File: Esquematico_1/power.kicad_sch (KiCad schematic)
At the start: 22 parts, among them U6 TPS54302DDCR, U7 AP2112K-3.3TRG1

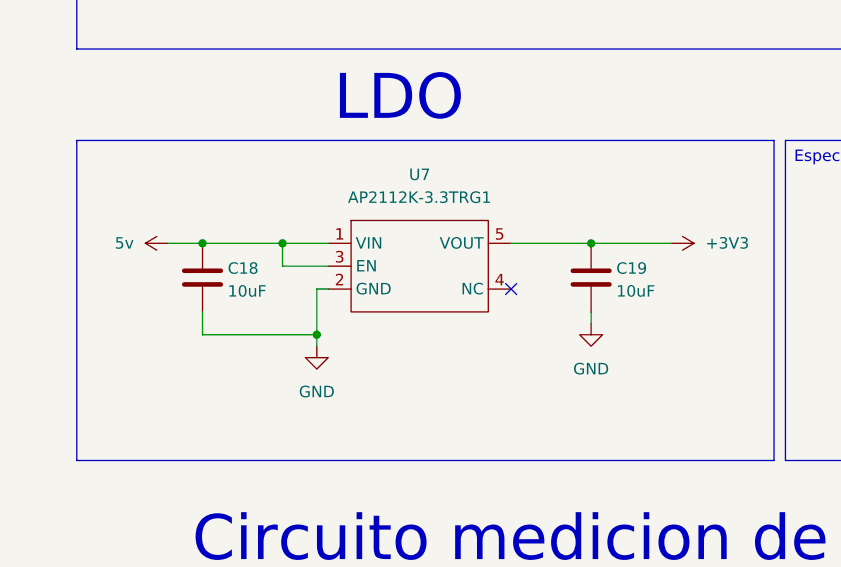
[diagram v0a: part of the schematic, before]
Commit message: Cambio del cristal por n-ésima vez
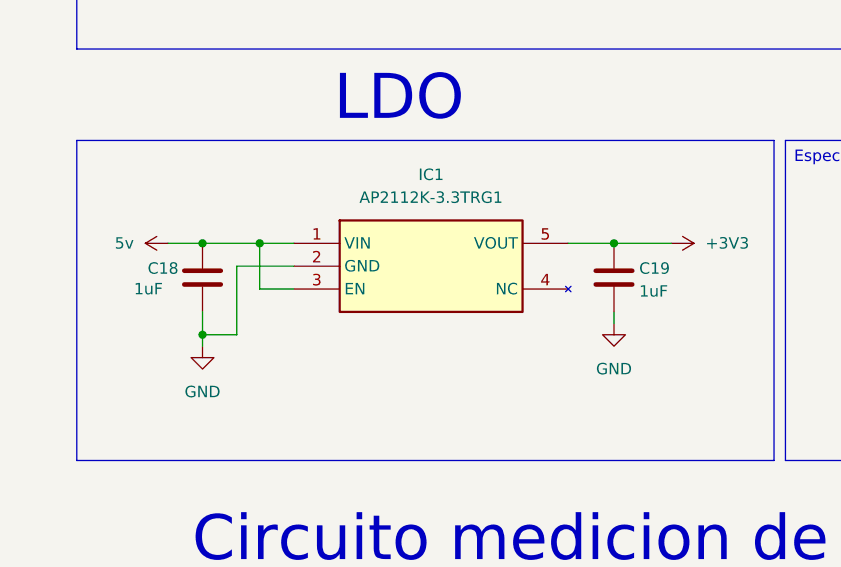
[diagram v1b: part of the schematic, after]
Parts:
- removed U7: AP2112K-3.3TRG1, AP2112K-3.3TRG1:SOT-23-6_L2.9-W1.6-P0.95-LS2.8-BL, symbol AP2112K-3.3TRG1:AP2112K-3.3TRG1_C23380830
- added IC1: AP2112K-3.3TRG1, AP2112K-3.3TRG1:SOT95P285X140-5N, symbol AP2112K-3_3TRG1:AP2112K-3.3TRG1
- C12, C13, C14, C15, C33: footprint (none) -> Capacitor_SMD:C_0805_2012Metric_Pad1.18x1.45mm_HandSolder
- C18, C19: value 10uF -> 1uF; footprint (none) -> Capacitor_SMD:C_0805_2012Metric_Pad1.18x1.45mm_HandSolder
- D1: footprint (none) -> Package_TO_SOT_SMD:SOT-23
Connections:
- net +3V3: now also IC1.5 (VOUT)
- net 5v: now also IC1.1 (VIN), IC1.3 (EN)
- net GND: now also IC1.2 (GND)
- no-connect marks 1 -> 0
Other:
- moved on the sheet: C19

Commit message: Footprints
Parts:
- C16, C17: footprint (none) -> Capacitor_SMD:C_0805_2012Metric_Pad1.18x1.45mm_HandSolder
- L1: footprint (none) -> Inductor_SMD:L_KOHERelec_MDA7030
- R10, R11, R12, R13, R17, R18, R9: footprint (none) -> Resistor_SMD:R_0805_2012Metric_Pad1.20x1.40mm_HandSolder
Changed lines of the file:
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@@
 			)
 		)
-		(property "Footprint" ""
+		(property "Footprint" "Inductor_SMD:L_KOHERelec_MDA7030"
 			(at 120.65 46.99 0)
 			(effects
@@
 			)
 		)
-		(property "Footprint" ""
+		(property "Footprint" "Resistor_SMD:R_0805_2012Metric_Pad1.20x1.40mm_HandSolder"
 			(at 156.972 59.69 90)
 			(effects
@@
 			)
 		)
-		(property "Footprint" ""
+		(property "Footprint" "Capacitor_SMD:C_0805_2012Metric_Pad1.18x1.45mm_HandSolder"
 			(at 133.6548 50.8 0)
 			(effects
@@
 			)
 		)
-		(property "Footprint" ""
+		(property "Footprint" "Resistor_SMD:R_0805_2012Metric_Pad1.20x1.40mm_HandSolder"
 			(at 156.972 68.58 90)
 			(effects
@@
 			)
 		)
-		(property "Footprint" ""
+		(property "Footprint" "Capacitor_SMD:C_0805_2012Metric_Pad1.18x1.45mm_HandSolder"
 			(at 127.3048 50.8 0)
 			(effects
@@
 			)
 		)
-		(property "Footprint" ""
+		(property "Footprint" "Resistor_SMD:R_0805_2012Metric_Pad1.20x1.40mm_HandSolder"
 			(at 68.072 162.56 90)
 			(effects
@@
 			)
 		)
-		(property "Footprint" ""
+		(property "Footprint" "Resistor_SMD:R_0805_2012Metric_Pad1.20x1.40mm_HandSolder"
 			(at 63.5 157.988 90)
 			(effects
@@
 			)
 		)
-		(property "Footprint" ""
+		(property "Footprint" "Resistor_SMD:R_0805_2012Metric_Pad1.20x1.40mm_HandSolder"
 			(at 50.292 46.99 90)
 			(effects
@@
 			)
 		)
-		(property "Footprint" ""
+		(property "Footprint" "Resistor_SMD:R_0805_2012Metric_Pad1.20x1.40mm_HandSolder"
 			(at 156.972 50.8 90)
 			(effects
@@
 			)
 		)
-		(property "Footprint" ""
+		(property "Footprint" "Resistor_SMD:R_0805_2012Metric_Pad1.20x1.40mm_HandSolder"
 			(at 50.292 36.83 90)
 			(effects

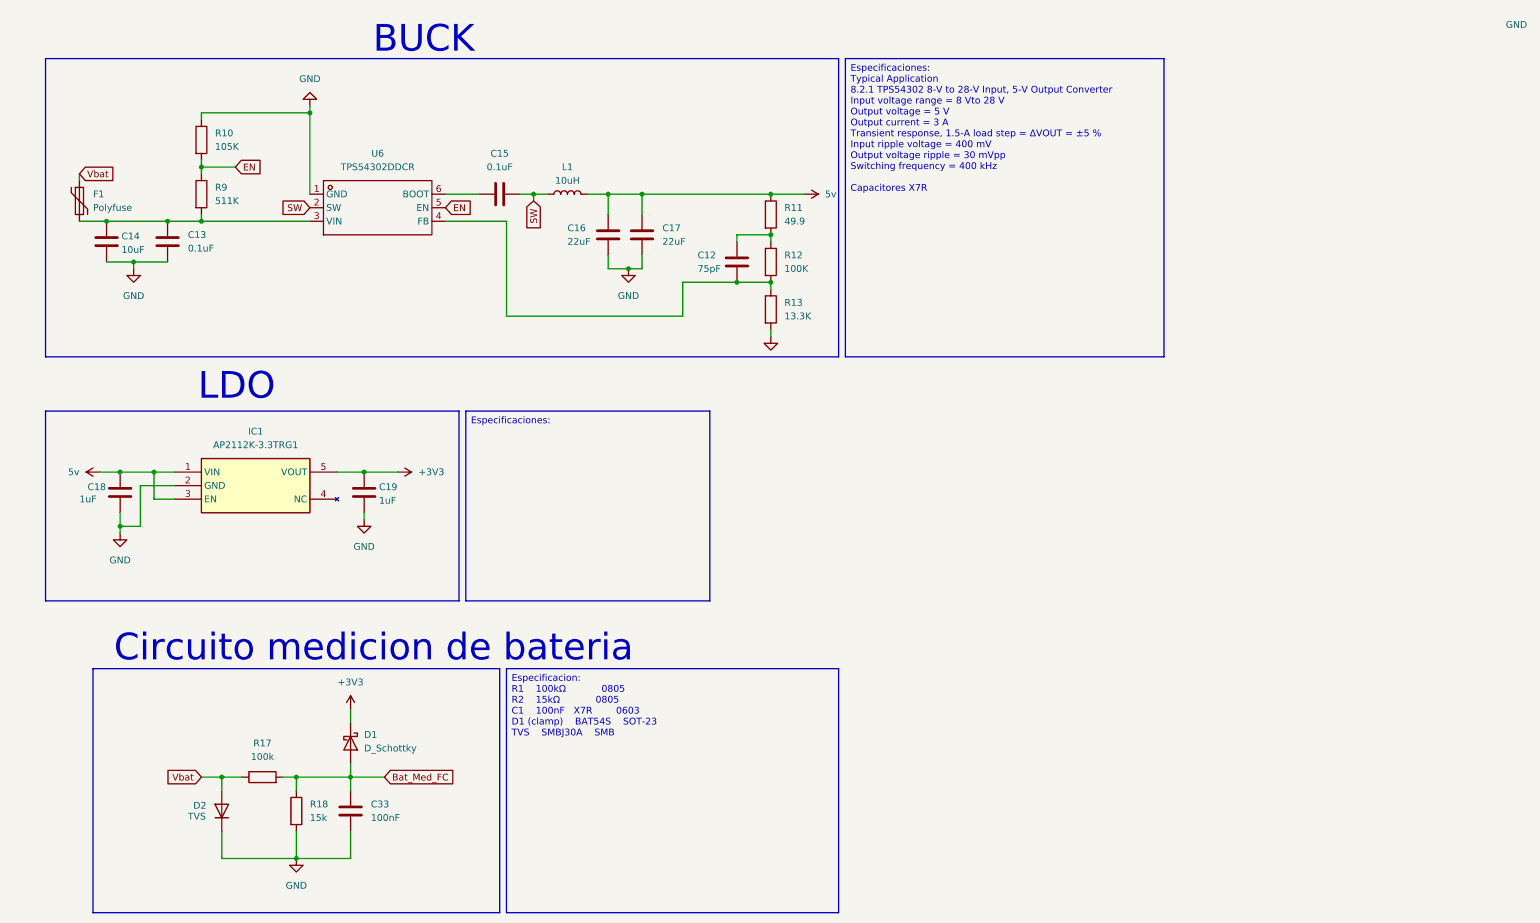
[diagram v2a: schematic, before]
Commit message: LDS y gran corrección de errores del esquemático
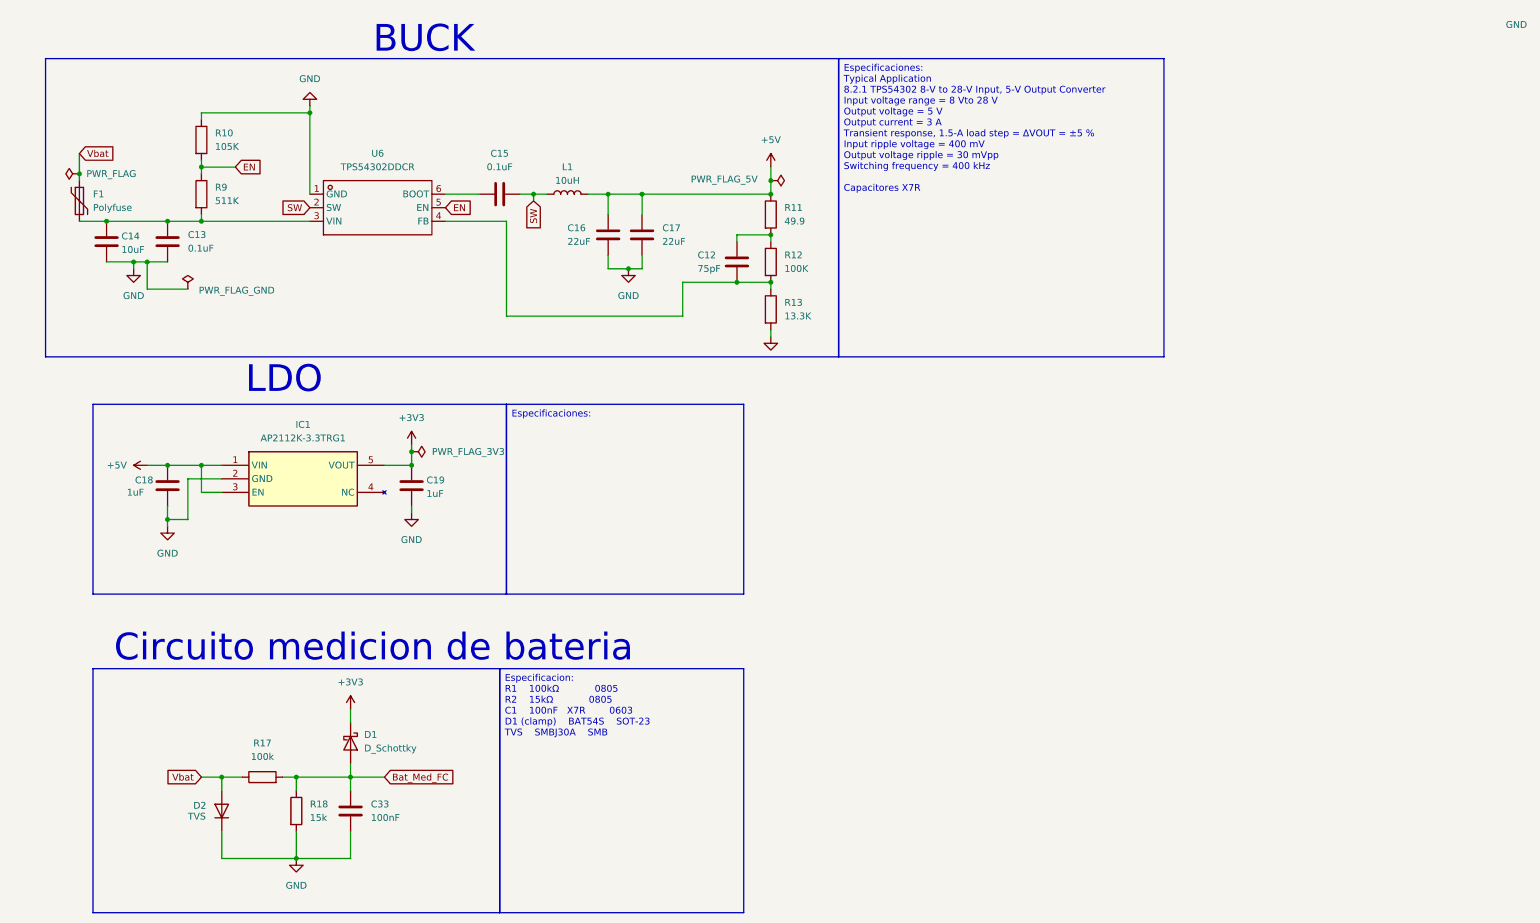
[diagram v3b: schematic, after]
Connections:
- net 5v renamed +5V
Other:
- moved on the sheet: C18, C19, IC1

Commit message: Todos los footprints menos ESC
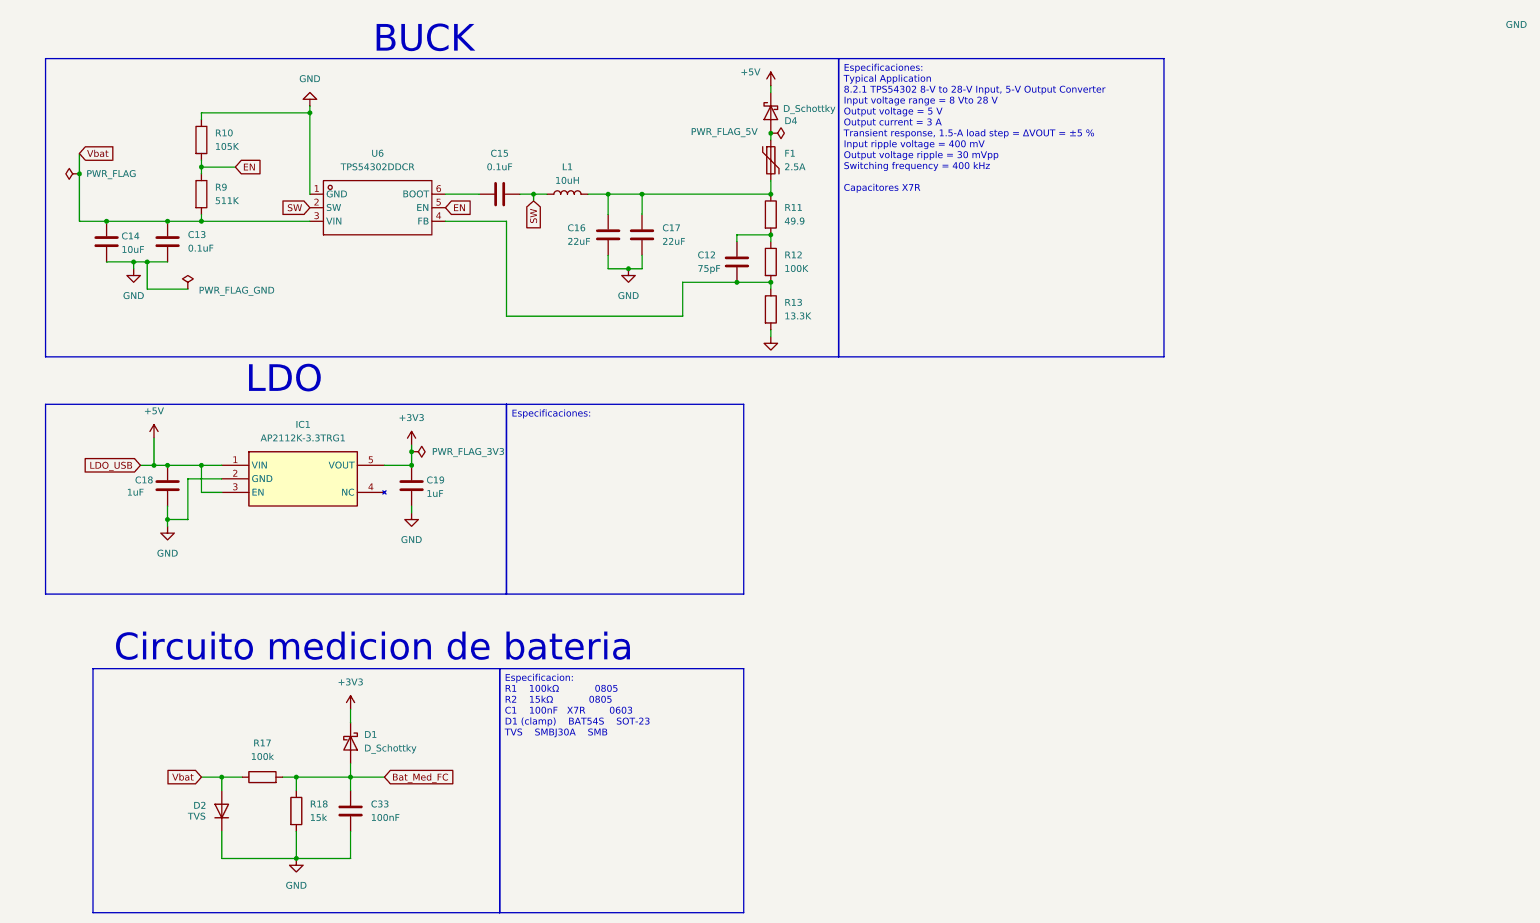
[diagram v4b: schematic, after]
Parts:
- added D4: D_Schottky, Package_TO_SOT_SMD:SOT-23, symbol Device:D_Schottky
- F1: value Polyfuse -> 2.5A; footprint (none) -> Fuse:Fuse_1812_4532Metric_Pad1.30x3.40mm_HandSolder
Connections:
- net +5V: now also D4.1 (K); no longer C16.2, C17.2, L1.2, R11.1
- net Vbat: now also C13.2, C14.2, R9.2, U6.3 (VIN); no longer F1.1
- new net: C16.2, C17.2, F1.2, L1.2, R11.1
- new net: D4.2 (A), F1.1
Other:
- moved on the sheet: F1
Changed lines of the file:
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@@
 	(text_box ""
 		(exclude_from_sim no)
-		(at 31.75 86.36 0)
-		(size 77.47 35.56)
+		(at 22.86 86.36 0)
+		(size 86.36 35.56)
 		(margins 0.9525 0.9525 0.9525 0.9525)
 		(stroke
@@
 	)
 	(junction
+		(at 43.18 97.79)
+		(diameter 0)
+		(color 0 0 0 0)
+	)
+	(junction
 		(at 45.72 52.07)
 		(diameter 0)
@@
 	)
 	(junction
+		(at 158.75 35.56)
+		(diameter 0)
+		(color 0 0 0 0)
+	)
+	(junction
 		(at 52.07 52.07)
 		(diameter 0)
@@
 		(color 0 0 0 0)
 	)
-	(junction
-		(at 158.75 44.45)
-		(diameter 0)
-		(color 0 0 0 0)
-	)
 	(wire
 		(pts
@@
 	(wire
 		(pts
+			(xy 158.75 35.56) (xy 158.75 36.83)
+		)
+		(stroke
+			(width 0)
+			(type default)
+		)
+	)
+	(wire
+		(pts
 			(xy 114.3 46.99) (xy 111.76 46.99)
 		)
@@
 	(wire
 		(pts
-			(xy 41.91 97.79) (xy 45.72 97.79)
+			(xy 55.88 100.33) (xy 49.53 100.33)
 		)
 		(stroke
@@
 	(wire
 		(pts
-			(xy 55.88 100.33) (xy 49.53 100.33)
+			(xy 45.72 107.95) (xy 45.72 105.41)
 		)
 		(stroke
@@
 	(wire
 		(pts
-			(xy 45.72 107.95) (xy 45.72 105.41)
+			(xy 158.75 26.67) (xy 158.75 27.94)
 		)
 		(stroke
@@
 	(wire
 		(pts
-			(xy 158.75 44.45) (xy 158.75 46.99)
-		)
-		(stroke
-			(width 0)
-			(type default)
-		)
-	)
-	(wire
-		(pts
 			(xy 29.21 39.37) (xy 29.21 43.18)
 		)
@@
 	(wire
 		(pts
-			(xy 29.21 43.18) (xy 29.21 44.45)
-		)
-		(stroke
-			(width 0)
-			(type default)
-		)
-	)
-	(wire
-		(pts
-			(xy 158.75 41.91) (xy 158.75 44.45)
+			(xy 34.29 59.69) (xy 39.37 59.69)
 		)
 		(stroke
@@
 	(wire
 		(pts
-			(xy 34.29 59.69) (xy 39.37 59.69)
+			(xy 158.75 73.66) (xy 158.75 72.39)
 		)
 		(stroke
@@
 	(wire
 		(pts
-			(xy 158.75 73.66) (xy 158.75 72.39)
+			(xy 45.72 97.79) (xy 52.07 97.79)
 		)
 		(stroke
@@
 	(wire
 		(pts
-			(xy 45.72 97.79) (xy 52.07 97.79)
+			(xy 43.18 97.79) (xy 45.72 97.79)
 		)
 		(stroke
@@
 	(wire
 		(pts
+			(xy 158.75 44.45) (xy 158.75 46.99)
+		)
+		(stroke
+			(width 0)
+			(type default)
+		)
+	)
+	(wire
+		(pts
+			(xy 43.18 97.79) (xy 40.64 97.79)
+		)
+		(stroke
+			(width 0)
+			(type default)
+		)
+	)
+	(wire
+		(pts
 			(xy 49.53 64.77) (xy 41.91 64.77)
 		)
@@
 	(wire
 		(pts
+			(xy 29.21 43.18) (xy 29.21 52.07)
+		)
+		(stroke
+			(width 0)
+			(type default)
+		)
+	)
+	(wire
+		(pts
 			(xy 55.88 166.37) (xy 55.88 171.45)
 		)
@@
 	(wire
 		(pts
+			(xy 43.18 92.71) (xy 43.18 97.79)
+		)
+		(stroke
+			(width 0)
+			(type default)
+		)
+	)
+	(wire
+		(pts
 			(xy 91.44 106.68) (xy 91.44 105.41)
 		)
@@
 		)
 	)
+	(global_label "LDO_USB"
+		(shape input)
+		(at 40.64 97.79 180)
+		(fields_autoplaced yes)
+		(effects
+			(font
+				(size 1.27 1.27)
+			)
+			(justify right)
+		)
+		(property "Intersheetrefs" "${INTERSHEET_REFS}"
+			(at 29.2486 97.79 0)
+			(effects
+				(font
+					(size 1.27 1.27)
+				)
+				(justify right)
+				(hide yes)
+			)
+		)
+	)
 	(global_label "EN"
 		(shape input)
@@
 	(symbol
 		(lib_id "power:+5V")
-		(at 158.75 41.91 0)
+		(at 158.75 26.67 0)
 		(unit 1)
 		(exclude_from_sim no)
@@
 		(on_board yes)
 		(dnp no)
-		(fields_autoplaced yes)
 		(property "Reference" "#PWR025"
-			(at 158.75 45.72 0)
+			(at 158.75 30.48 0)
 			(effects
 				(font
@@
 		)
 		(property "Value" "+5V"
-			(at 158.75 36.83 0)
+			(at 154.94 24.13 0)
 			(effects
 				(font
@@
 		)
 		(property "Footprint" ""
-			(at 158.75 41.91 0)
+			(at 158.75 26.67 0)
 			(effects
 				(font
@@
 		)
 		(property "Datasheet" ""
-			(at 158.75 41.91 0)
+			(at 158.75 26.67 0)
 			(effects
 				(font
@@
 		)
 		(property "Description" "Power symbol creates a global label with name \"+5V\""
-			(at 158.75 41.91 0)
+			(at 158.75 26.67 0)
 			(effects
 				(font
@@
 	)
 	(symbol
+		(lib_id "Device:D_Schottky")
+		(at 158.75 31.75 90)
+		(mirror x)
+		(unit 1)
+		(exclude_from_sim no)
+		(in_bom yes)
+		(on_board yes)
+		(dnp no)
+		(property "Reference" "D4"
+			(at 161.29 33.274 90)
+			(effects
+				(font
+					(size 1.27 1.27)
+				)
+				(justify right)
+			)
+		)
+		(property "Value" "D_Schottky"
+			(at 161.036 30.988 90)
+			(effects
+				(font
+					(size 1.27 1.27)
+				)
+				(justify right)
+			)
+		)
+		(property "Footprint" "Package_TO_SOT_SMD:SOT-23"
+			(at 158.75 31.75 0)
+			(effects
+				(font
+					(size 1.27 1.27)
+				)
+				(hide yes)
+			)
+		)
+		(property "Datasheet" "~"
+			(at 158.75 31.75 0)
+			(effects
+				(font
+					(size 1.27 1.27)
+				)
+				(hide yes)
+			)
+		)
+		(property "Description" "Schottky diode"
+			(at 158.75 31.75 0)
+			(effects
+				(font
+					(size 1.27 1.27)
+				)
+				(hide yes)
+			)
+		)
+		(pin "1"
+		)
+		(pin "2"
+		)
+		(instances
+			(project "Esquematico_1"
+				(path "/de2d80c1-c21c-478d-b724-17659b714c38/46661298-47a8-4fc3-89be-a6732b8d105c"
+					(reference "D4")
+					(unit 1)
+				)
+			)
+		)
+	)
+	(symbol
 		(lib_id "power:+3V3")
 		(at 80.01 143.51 0)
@@
 	(symbol
 		(lib_id "Device:Polyfuse")
-		(at 29.21 48.26 0)
+		(at 158.75 40.64 0)
 		(unit 1)
 		(exclude_from_sim no)
@@
 		(fields_autoplaced yes)
 		(property "Reference" "F1"
-			(at 31.75 46.9899 0)
+			(at 161.29 39.3699 0)
 			(effects
 				(font
@@
 			)
 		)
-		(property "Value" "Polyfuse"
-			(at 31.75 49.5299 0)
+		(property "Value" "2.5A"
+			(at 161.29 41.9099 0)
 			(effects
 				(font
@@
 			)
 		)
-		(property "Footprint" ""
-			(at 30.48 53.34 0)
+		(property "Footprint" "Fuse:Fuse_1812_4532Metric_Pad1.30x3.40mm_HandSolder"
+			(at 160.02 45.72 0)
 			(effects
 				(font
@@
 		)
 		(property "Datasheet" "~"
-			(at 29.21 48.26 0)
+			(at 158.75 40.64 0)
 			(effects
 				(font
@@
 		)
 		(property "Description" "Resettable fuse, polymeric positive temperature coefficient"
-			(at 29.21 48.26 0)
+			(at 158.75 40.64 0)
 			(effects
 				(font
@@
 		)
 		(instances
-			(project "power"
-				(path "/14e83f21-a583-4056-88d1-a5aa5c330b39"
-					(reference "F1")
-					(unit 1)
-				)
-			)
-			(project ""
+			(project "Esquematico_1"
 				(path "/de2d80c1-c21c-478d-b724-17659b714c38/46661298-47a8-4fc3-89be-a6732b8d105c"
 					(reference "F1")
@@
 	(symbol
 		(lib_id "power:PWR_FLAG")
-		(at 158.75 44.45 270)
+		(at 158.75 35.56 270)
 		(unit 1)
 		(exclude_from_sim no)
@@
 		(dnp no)
 		(property "Reference" "#FLG03"
-			(at 160.655 44.45 0)
+			(at 160.655 35.56 0)
 			(effects
 				(font
@@
 		)
 		(property "Value" "PWR_FLAG_5V"
-			(at 143.764 44.196 90)
+			(at 143.764 35.306 90)
 			(effects
 				(font
@@
 		)
 		(property "Footprint" ""
-			(at 158.75 44.45 0)
+			(at 158.75 35.56 0)
 			(effects
 				(font
@@
 		)
 		(property "Datasheet" "~"
-			(at 158.75 44.45 0)
+			(at 158.75 35.56 0)
 			(effects
 				(font
@@
 		)
 		(property "Description" "Special symbol for telling ERC where power comes from"
-			(at 158.75 44.45 0)
+			(at 158.75 35.56 0)
 			(effects
 				(font
@@
 	(symbol
 		(lib_id "power:+5V")
-		(at 41.91 97.79 90)
+		(at 43.18 92.71 0)
 		(unit 1)
 		(exclude_from_sim no)
@@
 		(fields_autoplaced yes)
 		(property "Reference" "#PWR052"
-			(at 45.72 97.79 0)
+			(at 43.18 96.52 0)
 			(effects
 				(font
@@
 		)
 		(property "Value" "+5V"
-			(at 38.1 97.7899 90)
+			(at 43.18 87.63 0)
 			(effects
 				(font
 					(size 1.27 1.27)
 				)
-				(justify left)
 			)
 		)
 		(property "Footprint" ""
-			(at 41.91 97.79 0)
+			(at 43.18 92.71 0)
 			(effects
 				(font
@@
 		)
 		(property "Datasheet" ""
-			(at 41.91 97.79 0)
+			(at 43.18 92.71 0)
 			(effects
 				(font
@@
 		)
 		(property "Description" "Power symbol creates a global label with name \"+5V\""
-			(at 41.91 97.79 0)
+			(at 43.18 92.71 0)
 			(effects
 				(font
